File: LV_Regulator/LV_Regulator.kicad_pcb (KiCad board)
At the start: 4 copper layers, 150 x 100 mm, 204 parts, among them IC1 UCC12040DVE, IC2 MIC29152WU, IC3 MIC29152WU, J1 430450400, J2 430450400, J3 430450800, J4 430450800, J5 SWD, J6 2169890001, K1 41.52.9.005.0010, Q1 BC807, U1 ADM2483xRW, U2 STM32F103C8Tx, U3 25CSM04xxSN, U4 BQ25858QWRRVRQ1, U5 CSD19506KTT, U6 CSD19506KTT, U7 CSD19506KTT, U8 CSD19506KTT, Y1 32.768kHz, Y2 8MHz

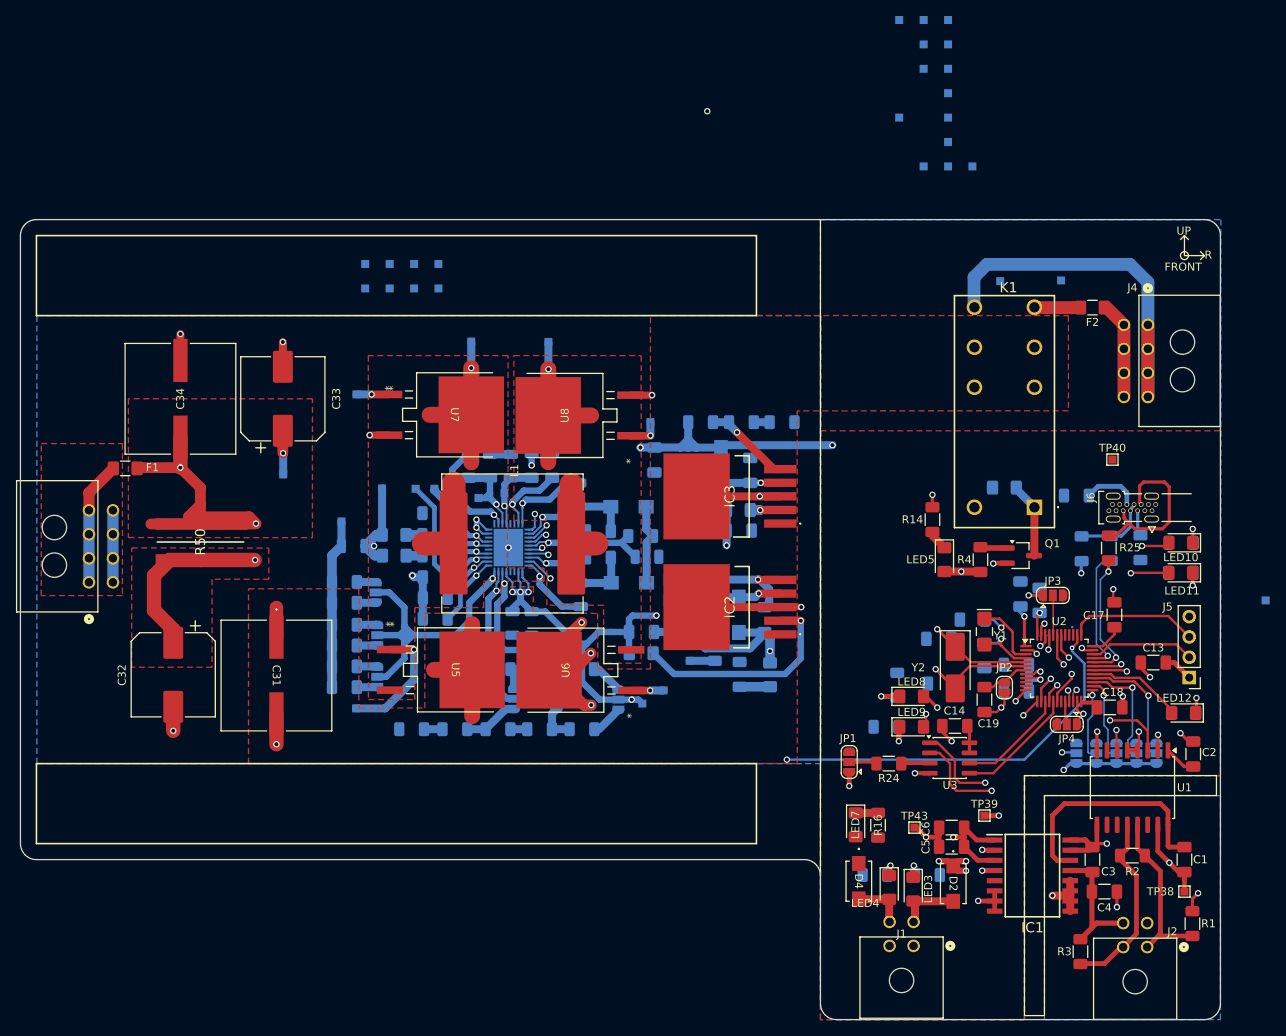
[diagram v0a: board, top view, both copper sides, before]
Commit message: Redesigned the control section of the LV_Regulator
The routing of the control section was redone completely, LED's were labeled with their function, some signals were renamed for consistency, removed redundant testpoints, removed names of testpoints, changed configuration jumpers to have human reada
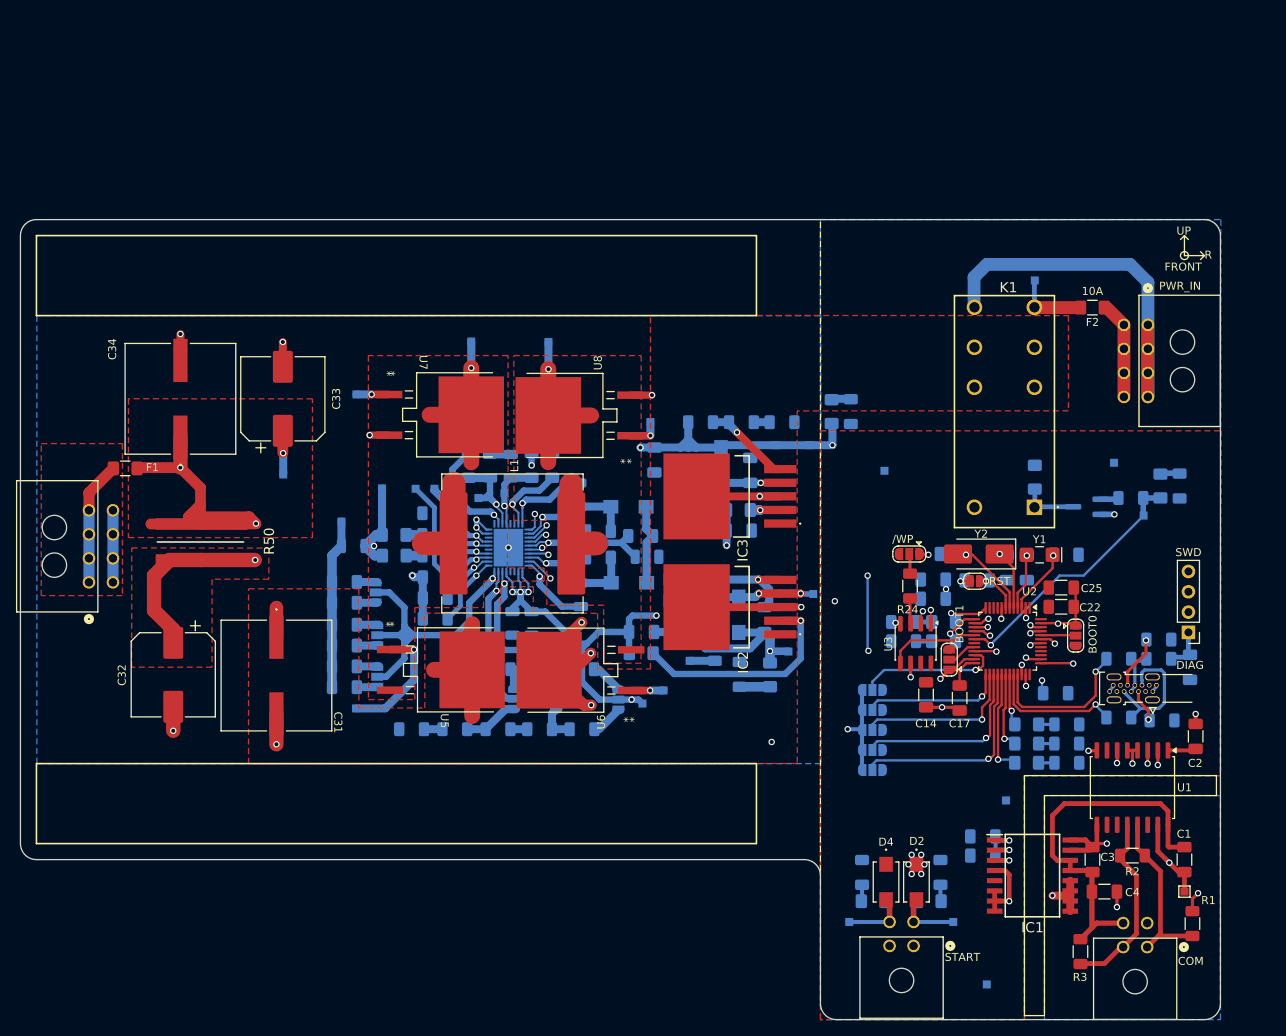
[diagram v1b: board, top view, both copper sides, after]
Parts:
- removed TP11: RS485-TX TP, TestPoint:TestPoint_Pad_1.0x1.0mm
- removed TP12: RS485-RX TP, TestPoint:TestPoint_Pad_1.0x1.0mm
- removed TP16, TP17, TP18, TP19, TP20, TP21, TP23, TP24, TP25, TP26, TP45, TP48: TestPoint, TestPoint:TestPoint_Pad_1.0x1.0mm
- 3V3: renamed from LED7; moved to B.Cu
- 3V3_EXT: renamed from LED4; moved to B.Cu
- 5V_EXT: renamed from LED3; moved to B.Cu
- C13, C18, C19, C5, C6, Q1, R14, R16, R25, R4, TP39, TP40, TP43: moved to B.Cu
- C22, C25: moved to F.Cu
- ERR: renamed from LED9; moved to B.Cu
- K1: renamed from LED5; moved to B.Cu
- OK: renamed from LED8; moved to B.Cu
- RUN: renamed from LED12; moved to B.Cu
- RX: renamed from LED10; moved to B.Cu
- TX: renamed from LED11; moved to B.Cu
- moved TP46 108.3 mm to (197.6, 131.8), turned to -90 degrees
- moved TP32 99.7 mm to (184.6, 131.8), turned to -90 degrees
- moved TP37 71.7 mm to (177.0, 98.0), turned to 90 degrees
- moved TP47 62.8 mm to (180.1, 90.8)
- moved TP22 58.2 mm to (221.4, 81.0), turned to 180 degrees
- moved TP43 52.0 mm to (217.7, 74.4), turned to 180 degrees
- moved R16 51.8 mm to (184.8, 68.0)
- moved 3V3 51.7 mm to (182.4, 68.0)
- moved TP49 46.5 mm to (175.4, 72.2)
- moved TP6 42.5 mm to (179.6, 72.2)
- moved TP44 41.0 mm to (204.2, 116.6)
- moved TP50 40.9 mm to (165.4, 74.8)
- moved ADR5 35.6 mm to (187.5, 112.8), turned to 180 degrees
- moved ADR4 33.0 mm to (187.5, 110.3), turned to 180 degrees
- moved R14 31.2 mm to (225.9, 77.3), turned to -90 degrees
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- renumbered JP1 to /WP, LED2 to 3V3_INT, LED6 to 5V, LED1 to 5V_INT, JP9 to ADR1, JP8 to ADR2, JP7 to ADR3, JP6 to ADR4, JP5 to ADR5, JP3 to BOOT0, JP4 to BOOT1, J2 to COM, J6 to DIAG, J4 to PWR_IN, JP2 to RST, J1 to START, J5 to SWD
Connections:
- net USB_DM renamed USB_DN
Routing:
- net SS: track 30.3 -> 11.5 mm
- net DIAG_RX: track 23.9 -> 6.51 mm, vias 2 -> 1
- net VBAT: track 118.2 -> 101.6 mm, vias 8 -> 6
- net INT_N: track 117.6 -> 102.9 mm, vias 2 -> 4
- net MISO_DOBROTO: track 30.3 -> 16.1 mm
- net CE_N: track 116.7 -> 102.7 mm
- net DIAG_ERR: track 16.4 -> 3.77 mm, vias 2 -> 1
- net SWDIO: track 13.3 -> 25.3 mm, vias 0 -> 1
- net DIAG_TX: track 21.6 -> 9.73 mm, vias 2 -> 1
- net ADR5: track 15.8 -> 26.6 mm
- net ADR3: track 10.7 -> 20.7 mm
- net DIAG_OK: track 14.3 -> 4.51 mm, vias 2 -> 1
- net ADR4: track 14.7 -> 23.5 mm
- net GND: track 138.3 -> 129.6 mm, vias 33 -> 25
- net ADR2: track 9.11 -> 17.7 mm
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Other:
- board text added: "10A"
